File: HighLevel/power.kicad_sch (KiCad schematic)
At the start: 27 parts, among them U17 MC74VHC1GT66, U18 MC74VHC1GT66, U19 MC74VHC1GT66

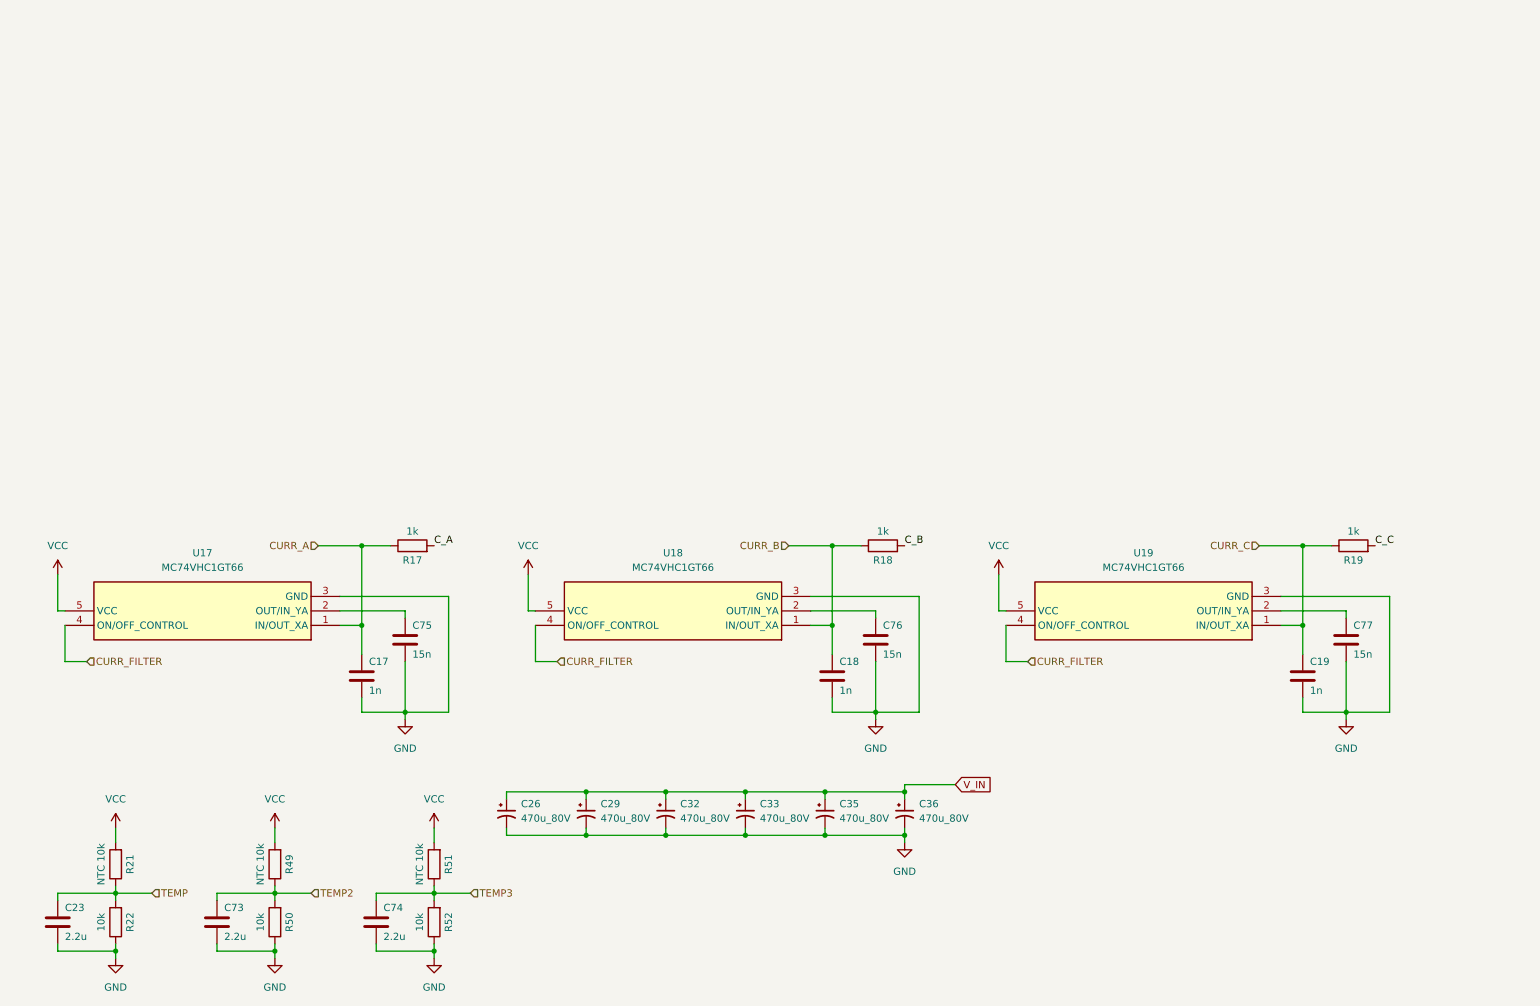
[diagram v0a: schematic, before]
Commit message: update: include footprints, remove previous power files
Fix Power file with updates, footprints included.
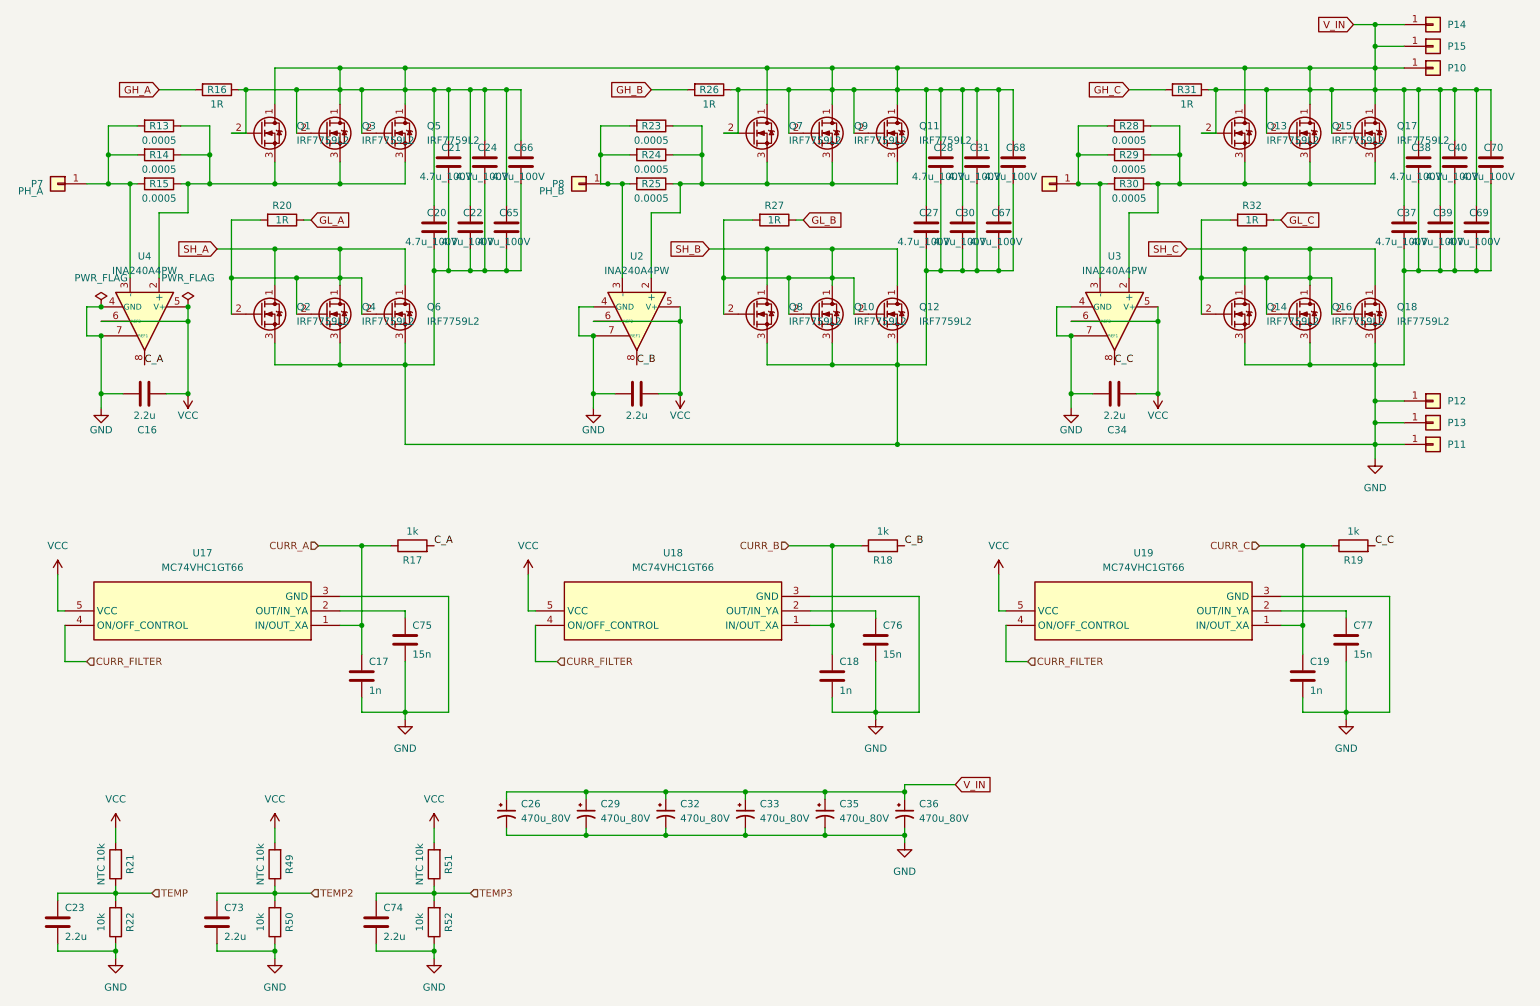
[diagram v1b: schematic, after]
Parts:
- added C16, C34, C4: 2.2u, Capacitor_SMD:C_0805_2012Metric, symbol Device:C
- added C20, C21, C22, C24, C27, C28, C30, C31, C37, C38, C39, C40, C65, C66, C67, C68, C69, C70: 4.7u_100V, Capacitor_SMD:C_0805_2012Metric, symbol Device:C
- added P10, P11, P12, P13, P14, P15: Conn_01x01, TestPoint:TestPoint_Pad_D2.5mm, symbol Connector_Generic:Conn_01x01
- added P7: PH_A, TestPoint:TestPoint_Pad_D2.5mm, symbol Connector_Generic:Conn_01x01
- added P8: PH_B, TestPoint:TestPoint_Pad_D2.5mm, symbol Connector_Generic:Conn_01x01
- added P9: PH_C, TestPoint:TestPoint_Pad_D2.5mm, symbol Connector_Generic:Conn_01x01
- added Q1, Q10, Q11, Q12, Q13, Q14, Q15, Q16, Q17, Q18, Q2, Q3, Q4, Q5, Q6, Q7, Q8, Q9: IRF7759L2, Package_DirectFET:DirectFET_L8, symbol Transistor_FET:IRF7759L2
- added R13, R23, R28: 0.0005, Capacitor_SMD:C_0805_2012Metric, symbol Device:R
- added R14, R15, R24, R25, R29, R30: 0.0005, Resistor_SMD:R_0805_2012Metric, symbol Device:R
- added R16, R20, R26, R27, R31, R32: 1R, Resistor_SMD:R_0805_2012Metric, symbol Device:R
- added U2, U3, U4: INA240A4PW, Package_SO:TSSOP-8_4.4x3mm_P0.65mm, symbol Amplifier_Current:INA240A4PW
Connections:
- net C_A: now also U4.8
- net C_B: now also U2.8
- net C_C: now also U3.8
- net GND: now also C16.2, C20.2, C21.2, C22.2, C24.2, C27.2, C28.2, C30.2, C31.2, C34.2, C37.2, C38.2, C39.2, C4.2, C40.2, C65.2, C66.2, C67.2, C68.2, C69.2, C70.2, P11.1 (Pin_1), P12.1 (Pin_1), P13.1 (Pin_1), Q10.3 (S), Q12.3 (S), Q14.3 (S), Q16.3 (S), Q18.3 (S), Q2.3 (S), Q4.3 (S), Q6.3 (S), Q8.3 (S), U2.1 (GND), U2.4 (GND), U2.7 (REF1), U3.1 (GND), U3.4 (GND), U3.7 (REF1), U4.1 (GND), U4.4 (GND), U4.7 (REF1)
- net VCC: now also C16.1, C34.1, C4.1, U2.5 (V+), U2.6 (REF2), U3.5 (V+), U3.6 (REF2), U4.5 (V+), U4.6 (REF2)
- net V_IN: now also C20.1, C21.1, C22.1, C24.1, C27.1, C28.1, C30.1, C31.1, C37.1, C38.1, C39.1, C40.1, C65.1, C66.1, C67.1, C68.1, C69.1, C70.1, P10.1 (Pin_1), P14.1 (Pin_1), P15.1 (Pin_1), Q1.1 (D), Q1.2 (G), Q11.1 (D), Q11.2 (G), Q13.1 (D), Q13.2 (G), Q15.1 (D), Q15.2 (G), Q17.1 (D), Q17.2 (G), Q3.1 (D), Q3.2 (G), Q5.1 (D), Q5.2 (G), Q7.1 (D), Q7.2 (G), Q9.1 (D), Q9.2 (G), R16.1, R26.1, R31.1
- new net: Q11.3 (S), Q7.3 (S), Q9.3 (S), R23.1, R24.1, R25.1, U2.2 (+)
- new net: Q13.3 (S), Q15.3 (S), Q17.3 (S), R28.1, R29.1, R30.1, U3.2 (+)
- new net: P9.1 (Pin_1), R28.2, R29.2, R30.2, U3.3 (-)
- new net: P7.1 (Pin_1), R13.2, R14.2, R15.2, U4.3 (-)
- new net: P8.1 (Pin_1), R23.2, R24.2, R25.2, U2.3 (-)
- new net: Q1.3 (S), Q3.3 (S), Q5.3 (S), R13.1, R14.1, R15.1, U4.2 (+)
- new net GH_A: R16.2
- new net GH_B: R26.2
- new net GH_C: R31.2
- new net GL_A: R20.1
- new net GL_B: R27.1
- new net GL_C: R32.1
- new net SH_A: Q2.1 (D), Q2.2 (G), Q4.1 (D), Q4.2 (G), Q6.1 (D), Q6.2 (G), R20.2
- new net SH_B: Q10.1 (D), Q10.2 (G), Q12.1 (D), Q12.2 (G), Q8.1 (D), Q8.2 (G), R27.2
- new net SH_C: Q14.1 (D), Q14.2 (G), Q16.1 (D), Q16.2 (G), Q18.1 (D), Q18.2 (G), R32.2
